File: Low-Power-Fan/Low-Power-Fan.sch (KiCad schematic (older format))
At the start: 9 parts, among them J1 in, J2 out, U1 FAN5333A

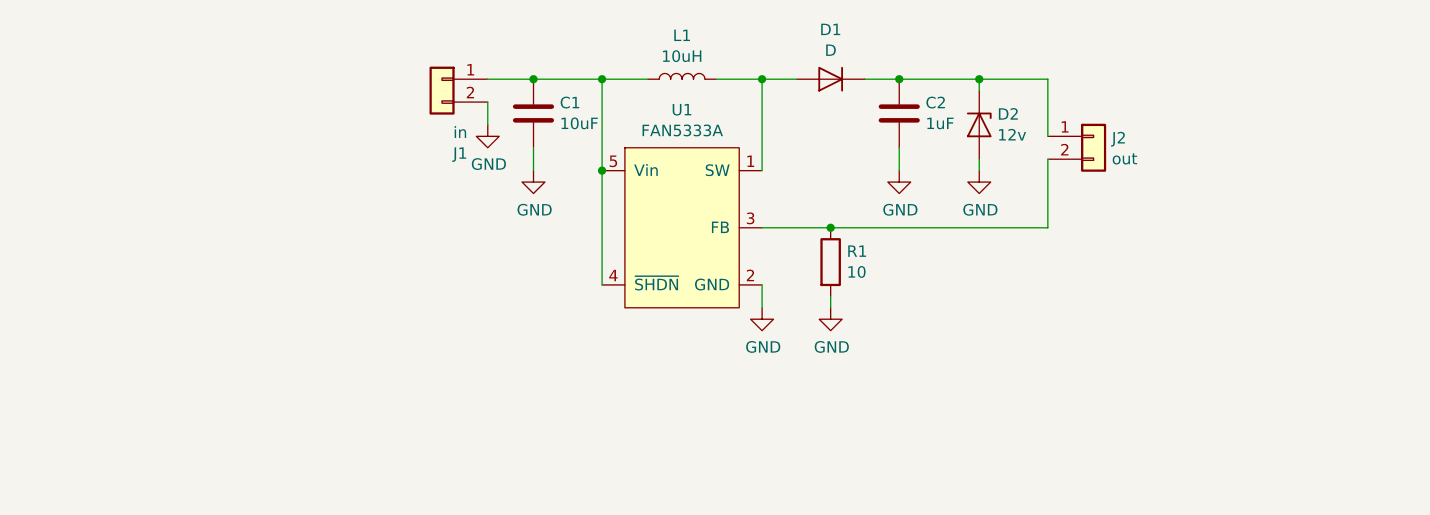
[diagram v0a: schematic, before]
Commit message: Added 10 minute timer and a switch. Updated resistor for higher current.
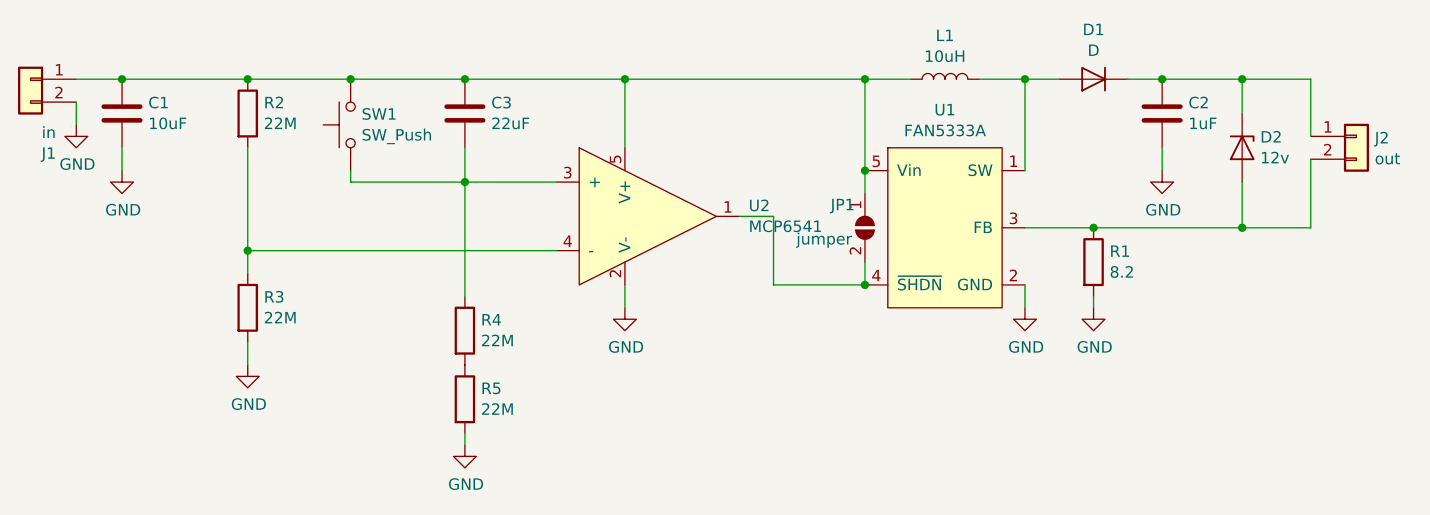
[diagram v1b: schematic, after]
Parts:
- added C3: 22uF, Capacitor_SMD:C_0603_1608Metric, symbol Device:C
- added JP1: jumper, Jumper:SolderJumper-2_P1.3mm_Open_Pad1.0x1.5mm, symbol Jumper:SolderJumper_2_Open
- added R2, R3, R4, R5: 22M, Resistor_SMD:R_0603_1608Metric, symbol Device:R
- added SW1: SW_Push, Button_Switch_SMD:SW_SPST_PTS645, symbol Switch:SW_Push
- added U2: MCP6541, Package_TO_SOT_SMD:SOT-23-5, symbol Low-Power-Fan:MCP6541
- R1: value 10 -> 8.2; footprint Resistor_SMD:R_0402_1005Metric -> Resistor_SMD:R_0603_1608Metric
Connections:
- net GND: now also R3.2, R5.2, U2.2 (V-); no longer D2.2 (A)
- net at J2.2 (Pin_2), R1.1, U1.3 (FB): now also D2.2 (A)
- net at C1.1, J1.1 (Pin_1), L1.1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: now also C3.1, JP1.1 (A), R2.1, SW1.2, U2.5 (V+); no longer U1.4 (~SHDN)
- new net: JP1.2 (B), U1.4 (~SHDN), U2.1
- new net: R4.2, R5.1
- new net: C3.2, R4.1, SW1.1, U2.3 (+)
- new net: R2.2, R3.1, U2.4 (-)
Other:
- moved on the sheet: C1, C2, D1, D2, J1, J2, L1, R1, U1

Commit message: Capacitor 3 replaced with correct size
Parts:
- C3: footprint Capacitor_SMD:C_0603_1608Metric -> Capacitor_SMD:C_0805_2012Metric
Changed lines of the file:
@@
 F 0 "C3" H 3415 3246 50  0000 L CNN
 F 1 "22uF" H 3415 3155 50  0000 L CNN
-F 2 "Capacitor_SMD:C_0603_1608Metric" H 3338 3050 50  0001 C CNN
+F 2 "Capacitor_SMD:C_0805_2012Metric" H 3338 3050 50  0001 C CNN
 F 3 "~" H 3300 3200 50  0001 C CNN
 	1    3300 3200

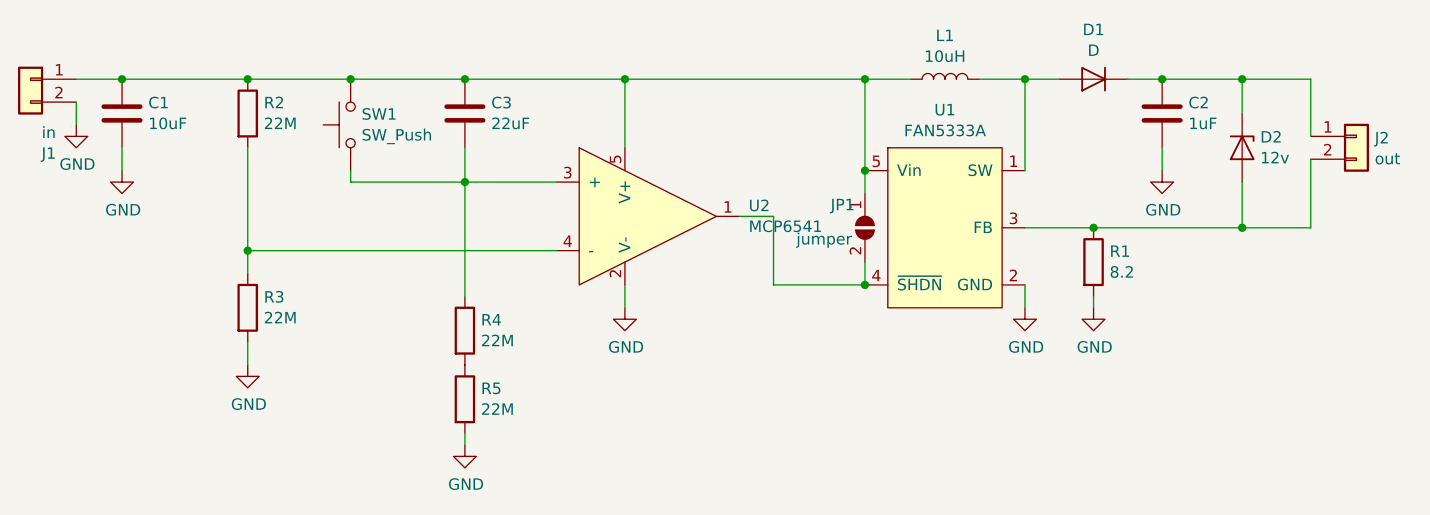
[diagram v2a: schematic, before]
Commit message: Connected one side of the capacitor to ground
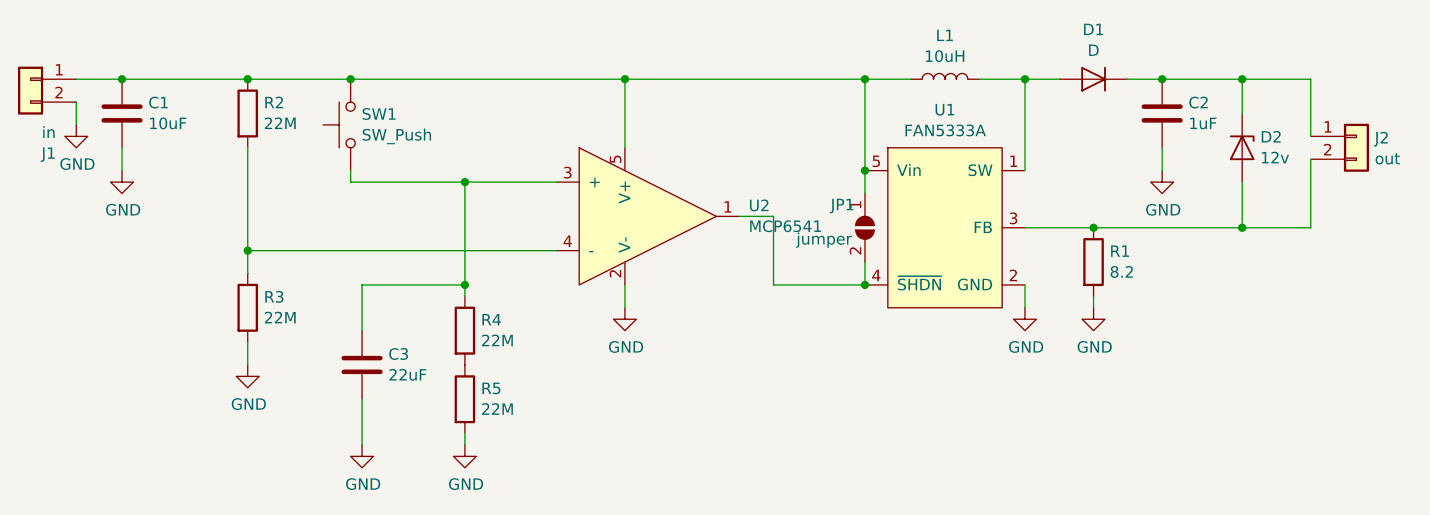
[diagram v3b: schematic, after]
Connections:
- net GND: now also C3.2
- net at C1.1, J1.1 (Pin_1), JP1.1 (A)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: no longer C3.1
- net at R4.1, SW1.1, U2.3 (+): now also C3.1; no longer C3.2
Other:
- moved on the sheet: C3
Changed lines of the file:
@@
 L Device:C C3
 U 1 1 5C4EA912
-P 3300 3200
-F 0 "C3" H 3415 3246 50  0000 L CNN
-F 1 "22uF" H 3415 3155 50  0000 L CNN
-F 2 "Capacitor_SMD:C_0805_2012Metric" H 3338 3050 50  0001 C CNN
-F 3 "~" H 3300 3200 50  0001 C CNN
-	1    3300 3200
+P 2850 4300
+F 0 "C3" H 2965 4346 50  0000 L CNN
+F 1 "22uF" H 2965 4255 50  0000 L CNN
+F 2 "Capacitor_SMD:C_0805_2012Metric" H 2888 4150 50  0001 C CNN
+F 3 "~" H 2850 4300 50  0001 C CNN
+	1    2850 4300
 	1    0    0    -1
 $EndComp
@@
 Connection ~ 1800 3050
 Connection ~ 2350 3050
-Connection ~ 3300 3050
-Wire Wire Line
-	3300 3050 4000 3050
 Connection ~ 3300 3500
-Wire Wire Line
-	3300 3500 3300 3350
 Connection ~ 2800 3050
-Wire Wire Line
-	2800 3050 3300 3050
 Wire Wire Line
 	2350 3050 2800 3050
@@
 	3700 3500 3300 3500
 Wire Wire Line
-	3300 3500 3300 4000
+	3300 3500 3300 3950
 Wire Wire Line
 	2800 3450 2800 3500
@@
 	1    0    0    -1
 $EndComp
+Wire Wire Line
+	2800 3050 4000 3050
+Wire Wire Line
+	2850 4150 2850 3950
+Wire Wire Line
+	2850 3950 3300 3950
+Connection ~ 3300 3950
+Wire Wire Line
+	3300 3950 3300 4000
+$Comp
+L power:GND #PWR?
+U 1 1 5C5C0E94
+P 2850 4650
+F 0 "#PWR?" H 2850 4400 50  0001 C CNN
+F 1 "GND" H 2855 4477 50  0000 C CNN
+F 2 "" H 2850 4650 50  0001 C CNN
+F 3 "" H 2850 4650 50  0001 C CNN
+	1    2850 4650
+	1    0    0    -1
+$EndComp
+Wire Wire Line
+	2850 4650 2850 4450
 $EndSCHEMATC

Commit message: Revert "Connected one side of the capacitor to ground"
This reverts commit a7569e6a569e54939577e6c551374c5e72ad59fc.
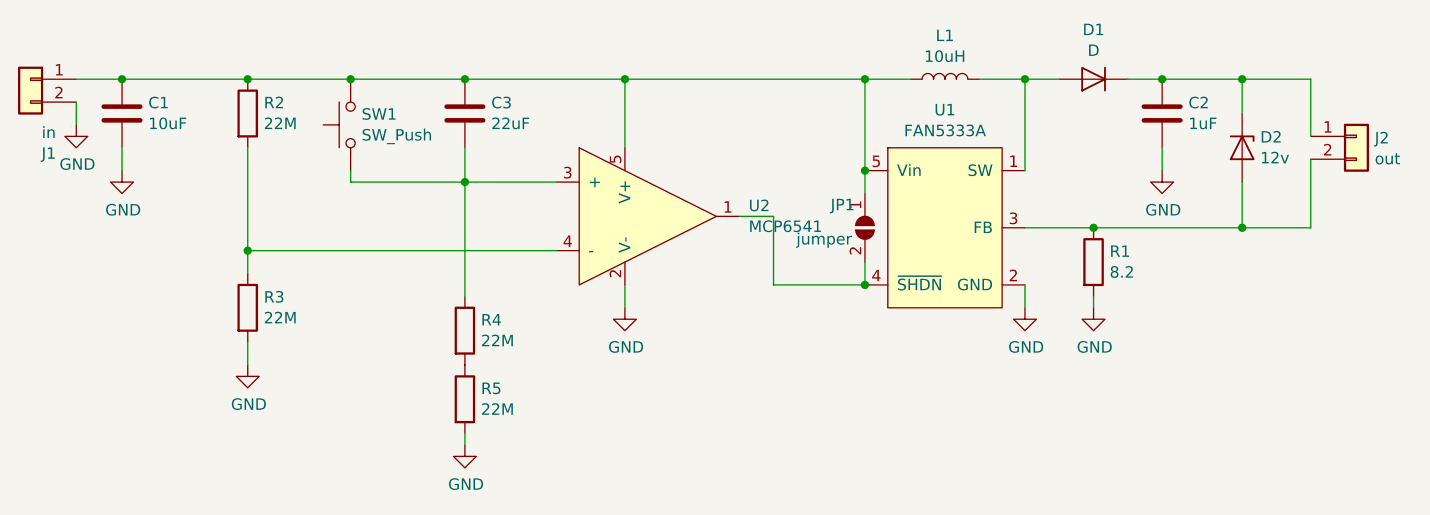
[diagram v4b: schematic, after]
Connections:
- net GND: no longer C3.2
- net at C1.1, J1.1 (Pin_1), JP1.1 (A)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: now also C3.1
- net at R4.1, SW1.1, U2.3 (+): now also C3.2; no longer C3.1
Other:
- moved on the sheet: C3
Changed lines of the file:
@@
 L Device:C C3
 U 1 1 5C4EA912
-P 2850 4300
-F 0 "C3" H 2965 4346 50  0000 L CNN
-F 1 "22uF" H 2965 4255 50  0000 L CNN
-F 2 "Capacitor_SMD:C_0805_2012Metric" H 2888 4150 50  0001 C CNN
-F 3 "~" H 2850 4300 50  0001 C CNN
-	1    2850 4300
+P 3300 3200
+F 0 "C3" H 3415 3246 50  0000 L CNN
+F 1 "22uF" H 3415 3155 50  0000 L CNN
+F 2 "Capacitor_SMD:C_0805_2012Metric" H 3338 3050 50  0001 C CNN
+F 3 "~" H 3300 3200 50  0001 C CNN
+	1    3300 3200
 	1    0    0    -1
 $EndComp
@@
 Connection ~ 1800 3050
 Connection ~ 2350 3050
+Connection ~ 3300 3050
+Wire Wire Line
+	3300 3050 4000 3050
 Connection ~ 3300 3500
+Wire Wire Line
+	3300 3500 3300 3350
 Connection ~ 2800 3050
+Wire Wire Line
+	2800 3050 3300 3050
 Wire Wire Line
 	2350 3050 2800 3050
@@
 	3700 3500 3300 3500
 Wire Wire Line
-	3300 3500 3300 3950
+	3300 3500 3300 4000
 Wire Wire Line
 	2800 3450 2800 3500
@@
 	1    0    0    -1
 $EndComp
-Wire Wire Line
-	2800 3050 4000 3050
-Wire Wire Line
-	2850 4150 2850 3950
-Wire Wire Line
-	2850 3950 3300 3950
-Connection ~ 3300 3950
-Wire Wire Line
-	3300 3950 3300 4000
-$Comp
-L power:GND #PWR?
-U 1 1 5C5C0E94
-P 2850 4650
-F 0 "#PWR?" H 2850 4400 50  0001 C CNN
-F 1 "GND" H 2855 4477 50  0000 C CNN
-F 2 "" H 2850 4650 50  0001 C CNN
-F 3 "" H 2850 4650 50  0001 C CNN
-	1    2850 4650
-	1    0    0    -1
-$EndComp
-Wire Wire Line
-	2850 4650 2850 4450
 $EndSCHEMATC
